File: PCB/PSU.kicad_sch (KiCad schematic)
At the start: 88 parts, among them Q1 2N7002, U1 AMS1117-3.3, U6 AP2127K-ADJ, U8 TUSB320LA, U9 TPS2557

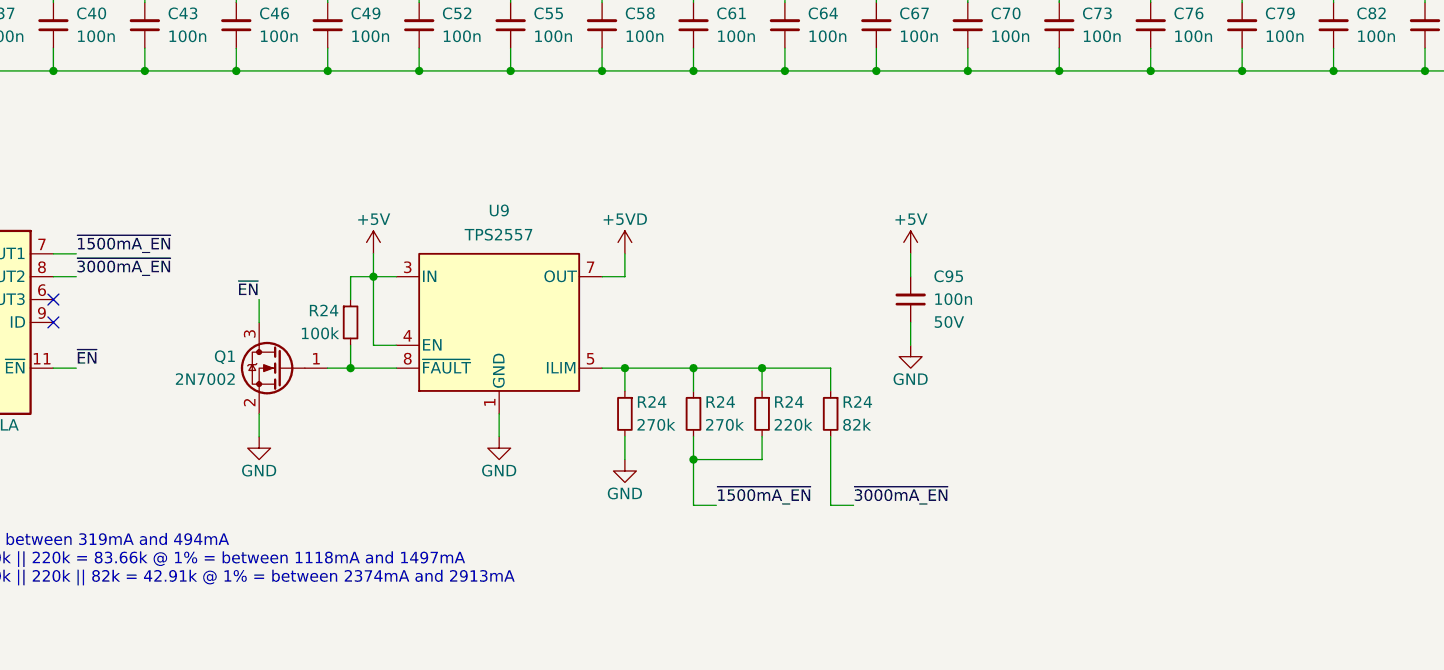
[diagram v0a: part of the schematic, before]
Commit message: Added large caps to output of TPS2557. Updated STEP file and file data.
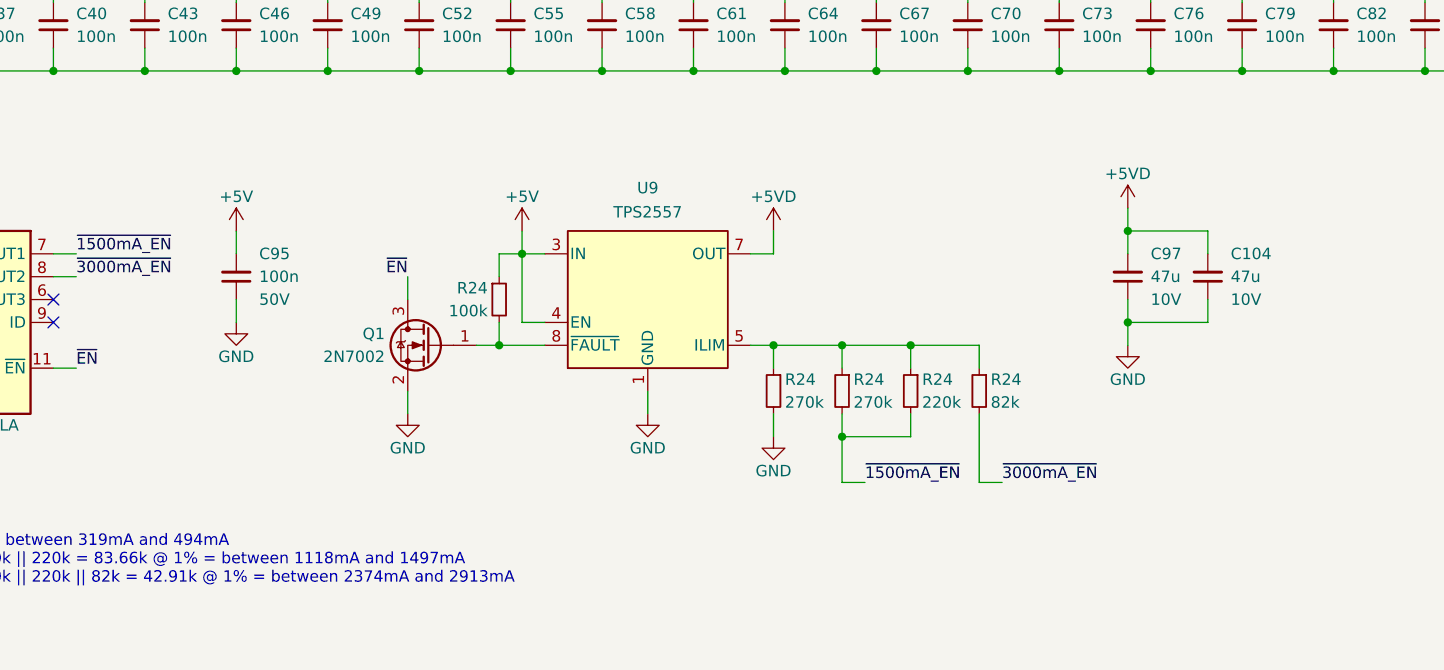
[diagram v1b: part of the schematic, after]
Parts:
- added C104, C97: 47u, Capacitor_SMD:C_1206_3216Metric, symbol Device:C_Small
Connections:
- net +5VD: now also C104.2, C97.2
- net GND: now also C104.1, C97.1
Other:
- company: (none) -> Created by Ariamelon (https://github.com/Ariamelon/Honeydew/)
- title: (none) -> Honeydew unified split ergonomic keyboard
- moved on the sheet: C95, Q1, R24, U9

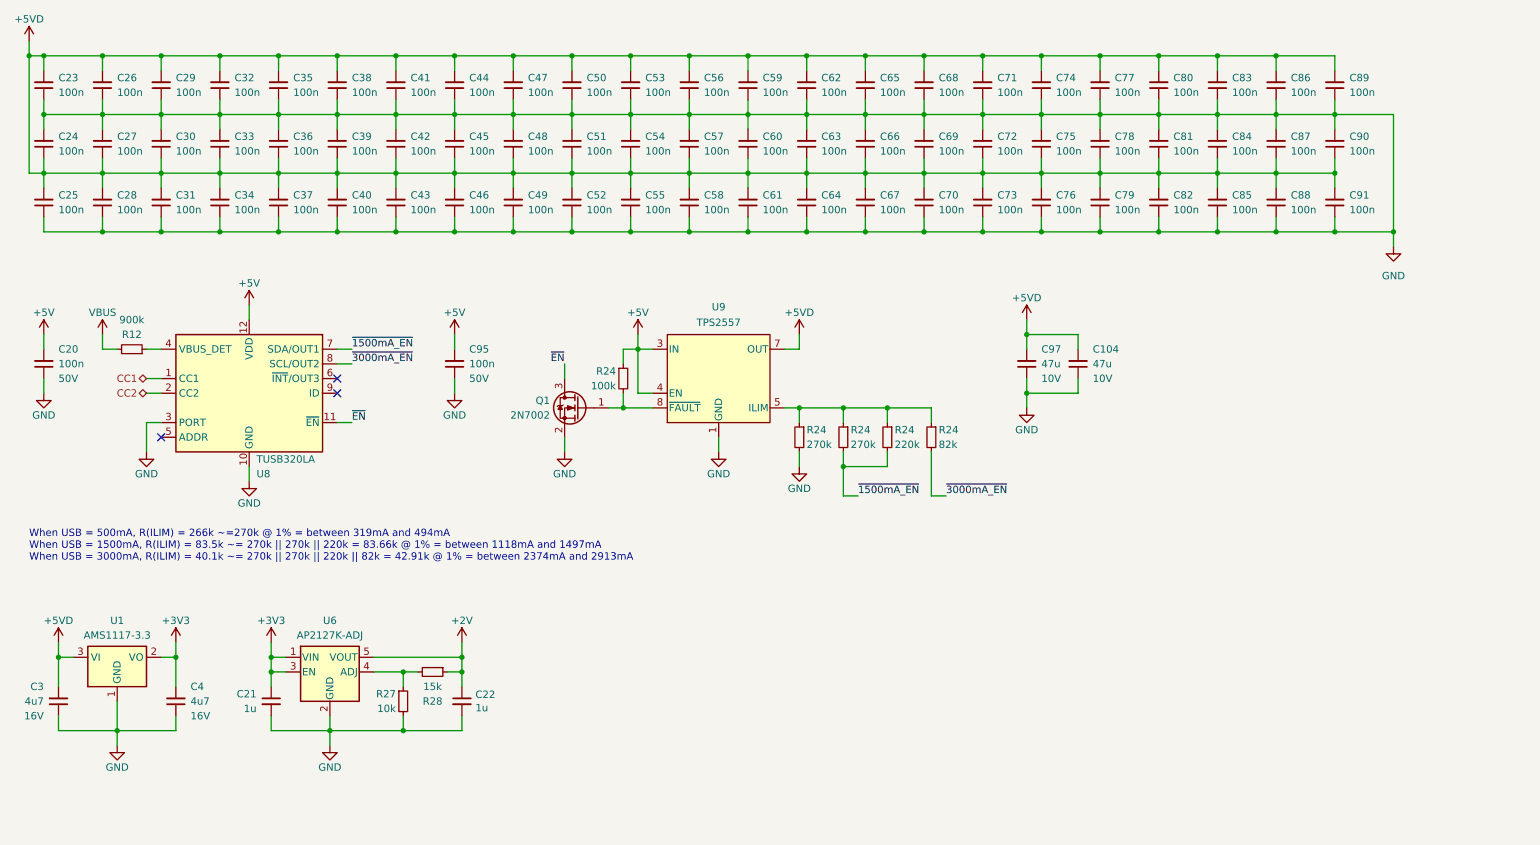
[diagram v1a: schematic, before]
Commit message: Shrunk size of PCB.
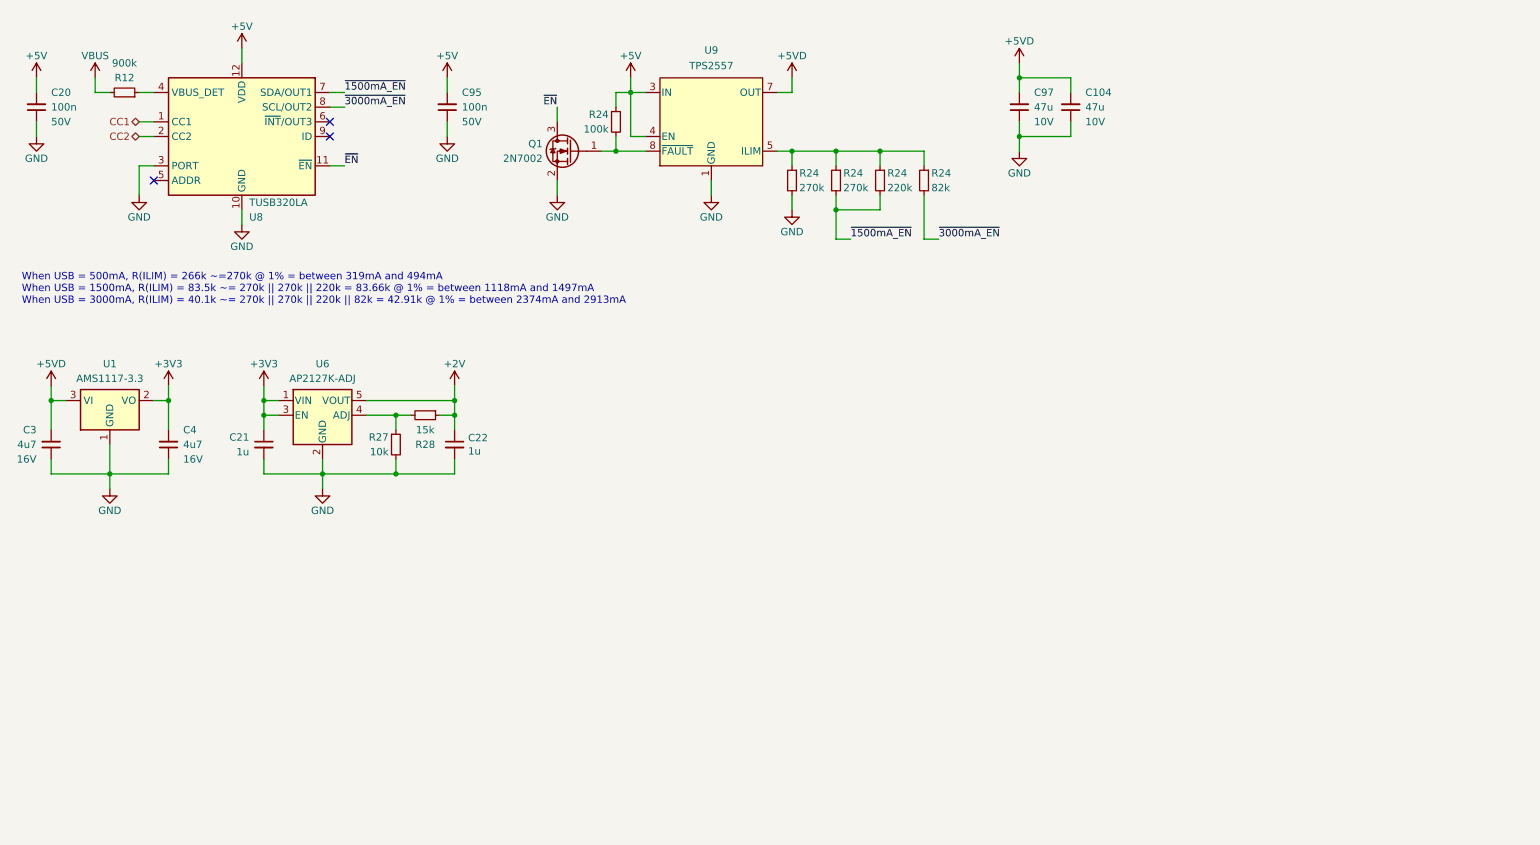
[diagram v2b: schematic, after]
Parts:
- removed C23, C24, C25, C26, C27, C28, C29, C30, C31, C32, C33, C34, C35, C36, C37, C38, C39, C40, C41, C42, C43, C44, C45, C46, C47, C48, C49, C50, C51, C52, C53, C54, C55, C56, C57, C58, C59, C60, C61, C62, C63, C64, C65, C66, C67, C68, C69, C70, C71, C72, C73, C74, C75, C76, C77, C78, C79, C80, C81, C82, C83, C84, C85, C86, C87, C88, C89, C90, C91: 100n, Honeydew:C_0402_1005Metric, symbol Device:C_Small
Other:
- moved on the sheet: C104, C20, C21, C22, C3, C4, C95, C97, Q1, R12, R24, R27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

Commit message: 17/04/2023 large update.
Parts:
- removed C104, C97: 47u, Capacitor_SMD:C_1206_3216Metric, symbol Device:C_Small
- removed C95: 100n, Capacitor_SMD:C_0402_1005Metric, symbol Device:C_Small
- removed Q1: 2N7002, Package_TO_SOT_SMD:SOT-23, symbol Transistor_FET:2N7002
- removed R24 (x2): 270k, Resistor_SMD:R_0402_1005Metric, symbol Device:R_Small
- removed R24: 82k, Resistor_SMD:R_0402_1005Metric, symbol Device:R_Small
- removed R24: 220k, Resistor_SMD:R_0402_1005Metric, symbol Device:R_Small
- removed R24: 100k, Resistor_SMD:R_0402_1005Metric, symbol Device:R_Small
- removed U1: AMS1117-3.3, Package_TO_SOT_SMD:SOT-223-3_TabPin2, symbol Regulator_Linear:AMS1117-3.3
- removed U9: TPS2557, Honeydew:HVSON-8-1EP_3x3mm_P0.65mm_EP1.6x2.4mm, symbol Honeydew:TPS2557
- added C1: 10n, Capacitor_SMD:C_0402_1005Metric, symbol Device:C_Small
- added C2: 1u, Capacitor_SMD:C_0603_1608Metric, symbol Device:C_Small
- added C23, C28: 100n, Capacitor_SMD:C_0402_1005Metric, symbol Device:C_Small
- added C35, C37: 4u7, Capacitor_SMD:C_0603_1608Metric, symbol Device:C_Small
- added C5: 22p, Capacitor_SMD:C_0402_1005Metric, symbol Device:C_Small
- added D1: 5V, Diode_SMD:D_SOD-523, symbol Device:D_Schottky_Small
- added D57: 1N5819WS, Diode_SMD:D_SOD-323, symbol Device:D_Small
- added FB1: 60R@100MHz, Inductor_SMD:L_0805_2012Metric, symbol Device:FerriteBead_Small
- added J1: USB In, Honeydew:HRO-TYPE-C-31-M-13x, symbol Connector:USB_C_Receptacle_USB2.0
- added L1: 10u, Inductor_SMD:L_Sunlord_SWPA3012S, symbol Device:L_Ferrite_Small
- added Q1, Q2, Q3: AO3400A, Package_TO_SOT_SMD:SOT-23, symbol Transistor_FET:AO3400A
- added R1 (x2), R15: 10k, Resistor_SMD:R_0402_1005Metric, symbol Device:R_Small
- added R16, R25: 1M, Resistor_SMD:R_0402_1005Metric, symbol Device:R_Small
- added R17: 330k, Resistor_SMD:R_0402_1005Metric, symbol Device:R_Small
- added R18, R19, R21: 4.7k, Resistor_SMD:R_0402_1005Metric, symbol Device:R_Small
- added R20: 3.3k, Resistor_SMD:R_0402_1005Metric, symbol Device:R_Small
- added R22: 2k, Resistor_SMD:R_0402_1005Metric, symbol Device:R_Small
- added R26: 100k, Resistor_SMD:R_0402_1005Metric, symbol Device:R_Small
- added U1: TPD4E05U06DQAR, Honeydew:USON-10_2.5x1.0mm_P0.5mm, symbol Casaba:TPD4E05U06DQAR
- added U12: TPS61040DBV, Package_TO_SOT_SMD:SOT-23-5, symbol Regulator_Switching:TPS61040DBV
- added U7: AMS1117-3.3, Package_TO_SOT_SMD:SOT-223-3_TabPin2, symbol Regulator_Linear:AMS1117-3.3
- added U9: TPS259533, Honeydew:WSON-8-1EP_2x2mm_P0.5mm_EP0.9x1.6mm, symbol Honeydew:TPS259533
- R12: value 900k -> 1M; LCSC C25905 -> C26083
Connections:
- net +5VD is gone; now on net +5V: C3.2
- net +3V3: now also U7.2 (VO)
- net +5V: now also C35.2, L1.2, R15.1, U12.4 (EN), U12.5 (VIN), U7.3 (VI), U9.5 (OUT); no longer C20.2, U8.12 (VDD)
- net CC1: now also J1.A5 (CC1), U1.5 (IO4), U1.6 (NC)
- net CC2: now also J1.B5 (CC2), U1.1 (IO1), U1.10 (NC)
- net GND: now also C1.1, C2.2, C23.1, C28.1, C35.1, C37.1, D1.2 (A), J1.A1 (GND), J1.A12 (GND), J1.B1 (GND), J1.B12 (GND), J1.S1 (SHIELD), Q1.2 (S), Q2.2 (S), Q3.2 (S), R1.1, R1.1, R17.2, R18.2, R26.2, U1.3 (GND), U1.8 (GND), U12.2 (GND), U7.1 (GND), U9.8 (GND), U9.9 (GND)
- net VBUS renamed IN
- net IN: now also C20.2, U8.12 (VDD), C2.1, C23.2, FB1.1, R16.1, U9.3 (IN), U9.4 (IN)
- net ~{1500mA_EN} renamed TUSB_OUT1
- net ~{3000mA_EN} renamed TUSB_OUT2
- net ~{EN}: no longer names the net of U8.11 (~{EN})
- net ~{EN}: now also Q1.3 (D)
- new net: C5.1, R25.1, R26.1, U12.3 (FB)
- new net: Q2.3 (D), R19.2, R20.2
- new net: D57.2 (A), L1.1, U12.1 (SW)
- new net: Q3.3 (D), R21.2, R22.2
- new net: C1.2, D1.1 (K), FB1.2, J1.A4 (VBUS), J1.A9 (VBUS), J1.B4 (VBUS), J1.B9 (VBUS)
- new net: C28.2, U9.1 (dVdt)
- new net: R16.2, R17.1, U9.2 (~{EN}/UVLO)
- new net +13V: C37.2, C5.2, D57.1 (K), R25.2
- new net 1500mA_EN: Q2.1 (G), R1.2
- new net 3000mA_EN: Q3.1 (G), R1.2
- new net D+: J1.A6 (D+), J1.B6 (D+), U1.2 (IO2), U1.9 (NC)
- new net D-: J1.A7 (D-), J1.B7 (D-), U1.4 (IO3), U1.7 (NC)
- new net ILIM_~{FLT}: Q1.1 (G), R15.2, U9.6 (~{FLT})
- new net I_SEN: R18.1, R19.1, R20.1, R21.1, R22.1, U9.7 (ILIM)
- no-connect marks 3 -> 5
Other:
- note added: "ADVERTISEMENT"
- note added: "Default current, attached"
- note added: "Default current, unattached"
- note added: "Default power (500mA): R(ILIM) = 4.7k @ 1% ~= 465mA"
- note added: "H"
- note added: "High current (3A), attached"
- note added: "High power (3000mA): R(ILIM) = 4.7k || 4.7k || 4.7k || 3.3k || 2k @ 1% = 693.8 ~= 2923mA"
- note added: "L"
- note added: "Med current (1.5A), attached"
- note added: "Med power (1500mA): R(ILIM) = 4.7k || 4.7k || 3.3k @ 1% = 1.37k ~= 1497mA"
- note added: "Note: ~{EN} is internally pulled up."
- note added: "OUT1"
- note added: "OUT2"
- note removed: "When USB = 500mA, R(ILIM) = 266k ~=270k @ 1% = between 319mA and 494mA When USB = 1500mA, R(ILIM) = 83.5k ~= 270k || 270k || 220k = 83.66k @ 1% = between 1118mA and 1497mA When USB = 3000mA, R(ILIM) = 40.1k ~= 270k || 270k || 220k || 82k = 42.91k @ 1% = between 2374mA and 2913mA"
- moved on the sheet: C20, C21, C22, C3, C4, R12, R27, R28, U6, U8
